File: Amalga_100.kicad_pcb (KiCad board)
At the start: 6 copper layers, 268 x 155 mm, 223 parts, among them IC1 ADM3052, IC3 INA240A1, IC4 INA240A1, IC5 INA240A1, P1 USB_B, P10 IN-, P2 Interface, P3 IN+, P4 IN-, P5 MOTOR3, P6 MOTOR2, P7 MOTOR1, P8 SWD, P9 CONN_6-HSWR-V2-rescue, Q1 IRFP4668PBF, Q10 IRFP4668PBF, Q11 IRFP4668PBF, Q12 IRFP4668PBF, Q13 BC846B, Q14 BC856B, Q15 BC846B, Q16 BC856B, Q2 IRFP4668PBF, Q3 IRFP4668PBF, Q4 IRFP4668PBF, Q5 IRFP4668PBF, Q6 IRFP4668PBF, Q7 IRFP4668PBF, Q8 IRFP4668PBF, Q9 IRFP4668PBF, SW1 SW_DIP_x02, U1 STM32F40X_LQFP64, U10 AD8664ARZ, U2 B1215S-2W, U3 JW5052C, U4 JW5052C, U5 ADUM3160, U6 AD2S1200YSTZ, U7 IRS2186, U8 IRS2186, U9 IRS2186, Y1 8MHz, Y2 8.912 MHZ

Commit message: made Bom (BomAmalga_Kosten.xlsx) Backup
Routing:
- net /Mosfet driver/H1_LOW: vias 62 -> 61
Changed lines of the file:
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@@
-(kicad_pcb (version 20171130) (host pcbnew "(5.0.1)-4")
+(kicad_pcb (version 20171130) (host pcbnew "(5.0.0)")
   (general
     (thickness 1.6)
     (drawings 95)
-    (tracks 3967)
+    (tracks 3965)
     (zones 0)
     (modules 223)
@@
     (tags "DIP Switch Slide 5.08mm 200mil Copal_CHS-A")
     (attr smd)
-    (fp_text reference SW1 (at 0 -2.965 270) (layer F.SilkS)
+    (fp_text reference SW1 (at 0 -0.2) (layer F.SilkS)
       (effects (font (size 1 1) (thickness 0.15)))
     )
@@
     (tags capacitor)
     (attr smd)
-    (fp_text reference C21 (at 0 -1.65 180) (layer F.SilkS)
+    (fp_text reference C21 (at 0.1 -1.9 180) (layer F.SilkS)
       (effects (font (size 1 1) (thickness 0.15)))
     )
@@
     (tags resistor)
     (attr smd)
-    (fp_text reference R67 (at 2.2625 1.6 180) (layer F.SilkS)
+    (fp_text reference R67 (at 2.4625 1.6 180) (layer F.SilkS)
       (effects (font (size 1 1) (thickness 0.15)))
     )
@@
     (tags capacitor)
     (attr smd)
-    (fp_text reference C37 (at -2.3375 0.6) (layer F.SilkS)
+    (fp_text reference C37 (at 2.7625 1) (layer F.SilkS)
       (effects (font (size 1 1) (thickness 0.15)))
     )
@@
     (tags capacitor)
     (attr smd)
-    (fp_text reference C40 (at 2.230367 1.1 180) (layer F.SilkS)
+    (fp_text reference C40 (at 2.230367 0.8 180) (layer F.SilkS)
       (effects (font (size 1 1) (thickness 0.15)))
     )
@@
     (tags resistor)
     (attr smd)
-    (fp_text reference R13 (at -2.330367 1.4) (layer F.SilkS)
+    (fp_text reference R13 (at -2.230367 0.6) (layer F.SilkS)
       (effects (font (size 1 1) (thickness 0.15)))
     )
@@
     (tags capacitor)
     (attr smd)
-    (fp_text reference C72 (at -2.8 1.4 180) (layer F.SilkS)
+    (fp_text reference C72 (at 0.1 1.5 180) (layer F.SilkS)
       (effects (font (size 1 1) (thickness 0.15)))
     )
@@
     (tags capacitor)
     (attr smd)
-    (fp_text reference C70 (at 0 -1.65) (layer F.SilkS)
+    (fp_text reference C70 (at -3 -0.2) (layer F.SilkS)
       (effects (font (size 1 1) (thickness 0.15)))
     )
@@
     (tags capacitor)
     (attr smd)
-    (fp_text reference C8 (at 2.687508 0.023924) (layer F.SilkS)
+    (fp_text reference C8 (at -0.512492 1.623924) (layer F.SilkS)
       (effects (font (size 1 1) (thickness 0.15)))
     )
@@
     (tags "SOIC 1.27")
     (attr smd)
-    (fp_text reference U10 (at -0.369028 2.773084 180) (layer F.SilkS)
+    (fp_text reference U10 (at -5.169028 2.273084 180) (layer F.SilkS)
       (effects (font (size 1 1) (thickness 0.15)))
     )
@@
     (tags SOT-23)
     (attr smd)
-    (fp_text reference Q14 (at -3.045647 1.618975 180) (layer F.SilkS)
+    (fp_text reference Q14 (at -3.345647 0.218975 180) (layer F.SilkS)
       (effects (font (size 1 1) (thickness 0.15)))
     )
@@
     (tags resistor)
     (attr smd)
-    (fp_text reference R42 (at 2.276076 -0.412492 180) (layer F.SilkS)
+    (fp_text reference R42 (at 2.276076 -0.712492 180) (layer F.SilkS)
       (effects (font (size 1 1) (thickness 0.15)))
     )
@@
     (tags resistor)
     (attr smd)
-    (fp_text reference R74 (at 0.2 -1.4625) (layer F.SilkS)
-      (effects (font (size 1 1) (thickness 0.15)))
+    (fp_text reference R74 (at -2.1 0.0375 90) (layer F.SilkS)
+      (effects (font (size 1 0.8) (thickness 0.15)))
     )
     (fp_text value 2K7 (at 0 1.65) (layer F.Fab)
@@
     (tags resistor)
     (attr smd)
-    (fp_text reference R76 (at 0 -1.65) (layer F.SilkS)
-      (effects (font (size 1 1) (thickness 0.15)))
+    (fp_text reference R76 (at -2.134259 0.5375 90) (layer F.SilkS)
+      (effects (font (size 1 0.8) (thickness 0.15)))
     )
     (fp_text value 33R (at 0 1.65) (layer F.Fab)
@@
     (tags resistor)
     (attr smd)
-    (fp_text reference R73 (at 0 -1.65 180) (layer F.SilkS)
+    (fp_text reference R73 (at -3.1 1.7625 180) (layer F.SilkS)
       (effects (font (size 1 1) (thickness 0.15)))
     )
@@
     (tags resistor)
     (attr smd)
-    (fp_text reference R69 (at -2.854353 1.581025) (layer F.SilkS)
+    (fp_text reference R69 (at -3.054353 1.381025) (layer F.SilkS)
       (effects (font (size 1 1) (thickness 0.15)))
     )
@@
     (tags resistor)
     (attr smd)
-    (fp_text reference R68 (at 2.369028 -0.273084 180) (layer F.SilkS)
+    (fp_text reference R68 (at 2.569028 -0.473084 180) (layer F.SilkS)
       (effects (font (size 1 1) (thickness 0.15)))
     )
@@
     (tags resistor)
     (attr smd)
-    (fp_text reference R39 (at -2.3375 1.3) (layer F.SilkS)
+    (fp_text reference R39 (at -0.0375 2.4) (layer F.SilkS)
       (effects (font (size 1 1) (thickness 0.15)))
     )
@@
   (segment (start 169.17003 151.35003) (end 170.674929 152.854929) (width 0.25) (layer "inner_layer4_(Sig)") (net 5))
   (via (at 210.7 80.8) (size 0.6) (drill 0.4) (layers "F.Cu_(top)" "B.Cu_(GND_bottom)") (net 6))
-  (via (at 213.82 92.2) (size 1) (drill 0.6) (layers "F.Cu_(top)" "B.Cu_(GND_bottom)") (net 6) (status 30))
   (segment (start 246.599358 110.411855) (end 236 110.411855) (width 0.25) (layer "F.Cu_(top)") (net 6))
   (segment (start 234.6 106.45) (end 234.6 108.1) (width 0.3) (layer "B.Cu_(GND_bottom)") (net 6) (status 10))
@@
   (segment (start 34.62501 163.87499) (end 34 164.5) (width 0.25) (layer "F.Cu_(top)") (net 163))
   (segment (start 34 164.5) (end 30.6 164.5) (width 0.25) (layer "F.Cu_(top)") (net 163))
-  (segment (start 36.8 161.5375) (end 37.4375 160.9) (width 0.25) (layer "F.Cu_(top)") (net 164))
   (segment (start 37.4375 160.9) (end 38.625 160.9) (width 0.25) (layer "F.Cu_(top)") (net 164))
-  (segment (start 36.6 161.8375) (end 36.8 161.6375) (width 0.25) (layer "F.Cu_(top)") (net 164))
-  (segment (start 36.6 164.1) (end 36.6 161.8375) (width 0.25) (layer "F.Cu_(top)") (net 164))
+  (segment (start 36.6 161.7) (end 37.1 161.2) (width 0.25) (layer "F.Cu_(top)") (net 164))
+  (segment (start 36.6 164.1) (end 36.6 161.7) (width 0.25) (layer "F.Cu_(top)") (net 164))
   (segment (start 35.7 165) (end 36.6 164.1) (width 0.25) (layer "F.Cu_(top)") (net 164))
   (segment (start 30.218147 165) (end 35.7 165) (width 0.25) (layer "F.Cu_(top)") (net 164))
@@
         (xy 61 91.103946) (xy 61.041322 91.104) (xy 61.041322 97.104) (xy 64.041322 100.104) (xy 76.041322 100.104)
         (xy 78.541322 97.604) (xy 78.5 94.75) (xy 91.958678 94.746) (xy 92.039398 100.502076) (xy 92 104)
-        (xy 87.8 108.4) (xy 59.4 108.4) (xy 58 107) (xy 58 84.4) (xy 55.8 82.2)
-        (xy 55.8 79.911341) (xy 61 79.911341)
+        (xy 87.8 108.4) (xy 59.4 108.4) (xy 58 107) (xy 58 90) (xy 61 90)
       )
     )
@@
     (polygon
       (pts
-        (xy 138 91.1) (xy 138.01 91.1) (xy 138.01 97.1) (xy 141.01 100.1) (xy 153.01 100.1)
+        (xy 138 90) (xy 138.01 91.1) (xy 138.01 97.1) (xy 141.01 100.1) (xy 153.01 100.1)
         (xy 155.51 97.6) (xy 155.51 94.5) (xy 169.01 94.5) (xy 169.008076 100.498076) (xy 169.01 103.6)
         (xy 164.2 108.4) (xy 136.4 108.4) (xy 135.01 107.1) (xy 135.01 100.1) (xy 135 100.1)
-        (xy 135 84.4) (xy 132.8 82.2) (xy 132.8 79.9) (xy 138 79.9)
+        (xy 135 90)
       )
     )
@@
         (xy 215.05 97) (xy 218.05 100) (xy 230.05 100) (xy 232.55 97.5) (xy 232.55 94.4)
         (xy 245.45 94.4) (xy 246.05 94.4) (xy 246.048076 100.398076) (xy 246.05 103.5) (xy 241.55 108)
-        (xy 213.05 108) (xy 212.05 107) (xy 212.05 84.3) (xy 209.75 82.2) (xy 209.8 79.900096)
-        (xy 215.1 79.899904)
+        (xy 213.05 108) (xy 212.05 107) (xy 212 90) (xy 215 90)
       )
     )

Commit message: added 2 mounting holes
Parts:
- removed the MH1 at (24.0, 187.0)
- removed SYM2: SYM_Arrow45_Tiny, Symbols:Symbol_Attention_CopperTop_Small
- added MH1: MountingHole, MountingHole:MountingHole_3.2mm_M3_ISO14580_Pad, F.Cu at (277.9, 17.5)
- added MH1: MountingHole, MountingHole:MountingHole_3.2mm_M3_ISO14580_Pad, F.Cu at (19.0, 17.0)
- added MH1: MountingHole, MountingHole:MountingHole_3.2mm_M3_ISO14580_Pad, F.Cu at (19.9, 162.5)
- C31, C32, C33: value 1u -> 1u 600V
- moved SYM1 137.1 mm to (264.6, 156.8)
- moved C53 84.4 mm to (110.8, 50.4)
- moved C51 77.3 mm to (187.9, 50.4)
- moved C50 25.0 mm to (32.4, 50.3)
- moved C19 24.8 mm to (158.0, 143.4)
- moved C27 24.8 mm to (263.9, 130.5)
- moved C41 24.8 mm to (248.3, 81.2)
- moved C5 24.8 mm to (269.4, 133.0)
- moved C54 24.8 mm to (104.9, 53.9)
- moved C61 24.8 mm to (258.9, 54.0)
- moved C62 24.8 mm to (171.3, 81.6)
- moved C63 24.8 mm to (272.9, 54.0)
- moved C66 24.8 mm to (181.9, 53.9)
- moved C69 24.8 mm to (200.4, 158.8)
- moved C7 24.8 mm to (269.4, 130.0)
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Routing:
- net H1_VS: track 159.8 -> 146.0 mm
- net H3_VS: track 221.4 -> 224.2 mm
- net GND: track 452.6 -> 451.2 mm, vias 51 -> 54
- net /MCU/SCK_ADC_EXT: track 164.5 -> 163.8 mm
- net /Resolver/Cos(S2): track 18.5 -> 18.7 mm, vias 1 -> 0
- net +BATT: vias 565 -> 557

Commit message: -tidied up resolver circuit (need voltage detection on reset pin. >10µs, low active)
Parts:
- removed the MH1 at (277.9, 17.5)
- removed the MH1 at (19.0, 17.0)
- added MH11: MountingHole, Mounting_Holes:MountingHole_3.2mm_M3_ISO14580_Pad, F.Cu at (19.0, 17.0)
- added MH12: MountingHole, Mounting_Holes:MountingHole_3.2mm_M3_ISO14580_Pad, F.Cu at (277.9, 17.5)
- MH1, MH2: footprint MountingHole:MountingHole_3.2mm_M3_ISO14580_Pad -> Mounting_Holes:MountingHole_3.2mm_M3_ISO14580_Pad
- MH10, MH3, MH4, MH5, MH6, MH7, MH8, MH9: footprint MountingHole:MountingHole_3.2mm_M3_ISO14580 -> Mounting_Holes:MountingHole_3.2mm_M3_ISO14580
- R61: value 442R -> 442R 1%
- R64: value 1K24 -> 1K24 1%
- U10: footprint Package_SO:SOIC-14_3.9x8.7mm_P1.27mm -> Housings_SOIC:SOIC-14_3.9x8.7mm_Pitch1.27mm
- moved C27 65.0 mm to (198.9, 131.4)
- moved C5 65.0 mm to (204.4, 133.9)
- moved C7 65.0 mm to (204.4, 130.9)
- moved L2 65.0 mm to (201.9, 126.4)
- moved R40 65.0 mm to (208.4, 134.4)
- moved R43 65.0 mm to (199.9, 134.4)
- moved R44 65.0 mm to (197.9, 134.4)
- moved U4 65.0 mm to (204.4, 133.9)
- moved C45 0.65 mm to (68.5, 120.3)
- moved C46 0.56 mm to (104.3, 120.1)
- moved C48 0.25 mm to (53.4, 120.3)
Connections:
- IC1 pad 10: Net-(IC1-Pad10) -> (no net)
- P8 pad 6: Net-(P8-Pad6) -> (no net)
- Q13 pad 3: +12V -> +15V
- Q15 pad 3: +12V -> +15V
- U1 pad 2: Net-(U1-Pad2) -> (no net)
- U1 pad 25: Net-(U1-Pad25) -> (no net)
- U1 pad 28: Net-(U1-Pad28) -> (no net)
- U1 pad 3: Net-(U1-Pad3) -> (no net)
- U1 pad 33: Net-(U1-Pad33) -> (no net)
- U1 pad 4: Net-(U1-Pad4) -> (no net)
- U1 pad 53: Net-(U1-Pad53) -> (no net)
- U1 pad 54: Net-(U1-Pad54) -> (no net)
- U6 pad 10: Net-(U6-Pad10) -> (no net)
- U6 pad 11: Net-(U6-Pad11) -> (no net)
- U6 pad 12: Net-(U6-Pad12) -> (no net)
- U6 pad 13: Net-(U6-Pad13) -> (no net)
- U6 pad 14: Net-(U6-Pad14) -> (no net)
- U6 pad 15: Net-(U6-Pad15) -> (no net)
- U6 pad 16: Net-(U6-Pad16) -> GND
- U6 pad 18: Net-(U6-Pad18) -> (no net)
- U6 pad 19: Net-(U6-Pad19) -> (no net)
- U6 pad 20: Net-(U6-Pad20) -> (no net)
- U6 pad 24: Net-(U6-Pad24) -> (no net)
- U6 pad 29: Net-(U6-Pad29) -> (no net)
- U6 pad 30: Net-(U6-Pad30) -> (no net)
- U6 pad 33: Net-(U6-Pad33) -> (no net)
- U6 pad 44: Net-(U6-Pad44) -> (no net)
- U6 pad 9: Net-(U6-Pad9) -> (no net)
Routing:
- net +15V: track 528.0 -> 492.2 mm, vias 9 -> 10
- net +12V: track 25.9 -> 0.00 mm
- net +3V3: track 620.7 -> 607.8 mm, vias 14 -> 15
- net H1_VS: track 146.0 -> 152.8 mm
- net GND: track 451.2 -> 448.5 mm, vias 54 -> 53
- net GNDPWR: track 81.9 -> 84.2 mm
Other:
- board text added: "Amalga 600V 150A *20190213"
- board text added: "prim. to sec. Ohm 1:2 100k 1:1 40k 2:1 10k 5:1"
- board text removed: "Amalga 200 600V 150A *20190213 -Orig A.S."
- board text removed: "prim. to sec. Ohm 1:1 100k 2:1 40k 5:1 10k"

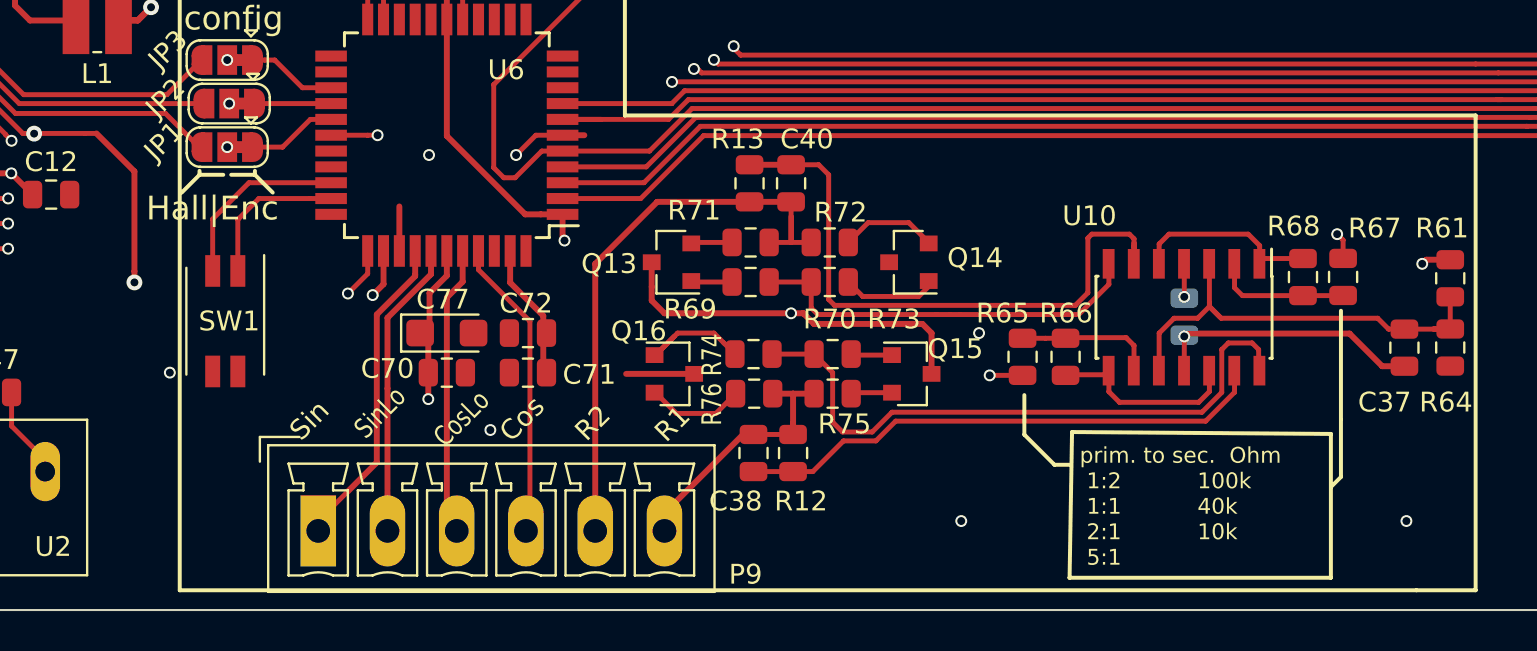
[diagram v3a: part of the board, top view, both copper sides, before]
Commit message: -started implementing new sin/cos-Encoder Inputs -small changes like silkscreen
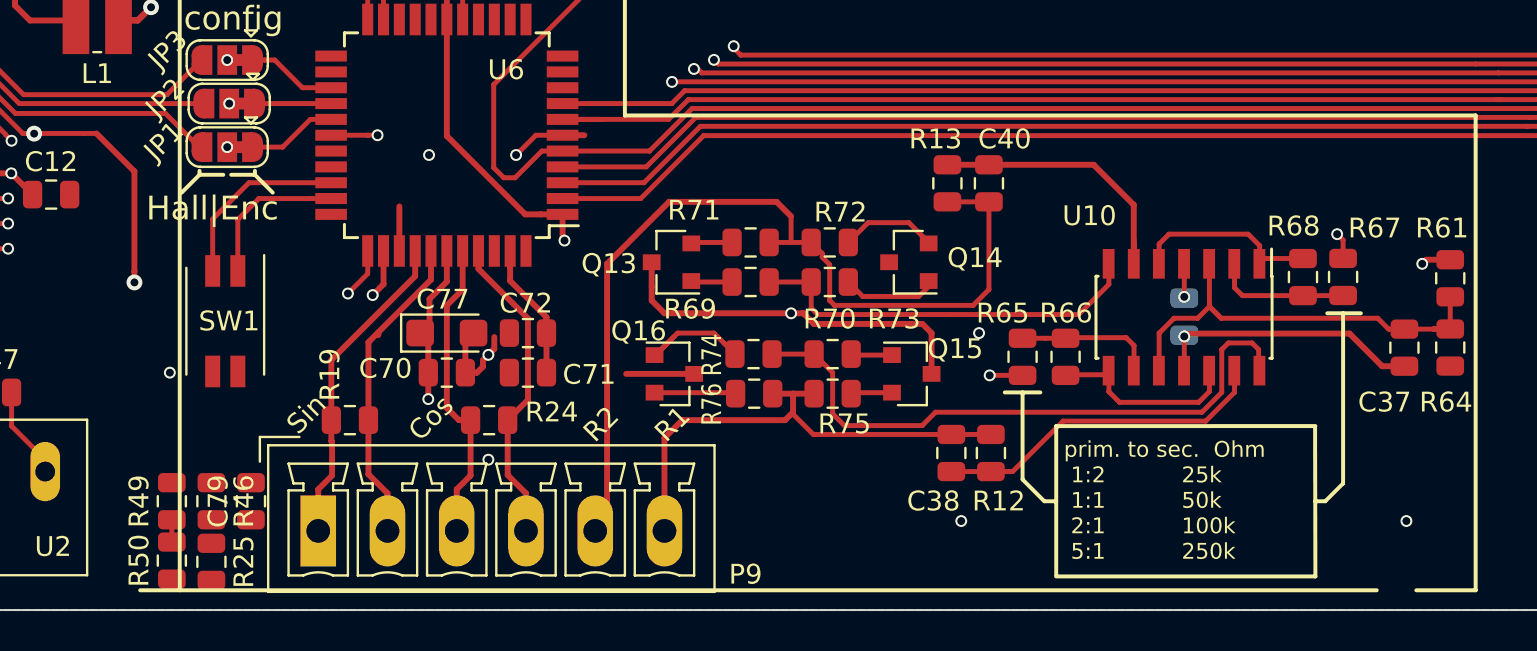
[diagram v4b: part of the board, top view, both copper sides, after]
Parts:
- added C79: 10nF, Capacitor_SMD:C_0805_2012Metric, F.Cu at (80.0, 162.0)
- added R19: 68k, Resistor_SMD:R_0805_2012Metric, F.Cu at (85.0, 157.9)
- added R24: 68k, Resistor_SMD:R_0805_2012Metric, F.Cu at (92.0, 157.9)
- added R25: 68k, Resistor_SMD:R_0805_2012Metric, F.Cu at (78.0, 165.1)
- added R46: 68k, Resistor_SMD:R_0805_2012Metric, F.Cu at (78.0, 162.0)
- added R49: 68k, Resistor_SMD:R_0805_2012Metric, F.Cu at (76.0, 162.0)
- added R50: 68k, Resistor_SMD:R_0805_2012Metric, F.Cu at (76.0, 165.0)
- R65, R67: value ?R -> 100k 1%
- R66, R68: value ?R -> 25k 1%
- moved C38 10.0 mm to (115.4, 159.6)
- moved C40 10.0 mm to (117.3, 145.9)
- moved R12 10.0 mm to (117.4, 159.6)
- moved R13 10.0 mm to (115.2, 145.9)
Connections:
- net SPI1_SCK(R2D) renamed SPI1_SCK_(R2D)
- IC1 pad 10: (no net) -> Net-(IC1-Pad10)
- P8 pad 6: (no net) -> Net-(P8-Pad6)
- U1 pad 2: (no net) -> /Resolver/*RDvel
- U1 pad 25: (no net) -> Net-(U1-Pad25)
- U1 pad 26: /Resolver/*CS -> /MCU/SIN_IN_RES
- U1 pad 27: /Resolver/*RDvel -> /MCU/COS_IN_RES
- U1 pad 28: (no net) -> Net-(U1-Pad28)
- U1 pad 3: (no net) -> Net-(U1-Pad3)
- U1 pad 33: (no net) -> Net-(U1-Pad33)
- U1 pad 4: (no net) -> Net-(U1-Pad4)
- U1 pad 53: (no net) -> /Resolver/*CS
- U1 pad 54: (no net) -> Net-(U1-Pad54)
- U6 pad 10: (no net) -> Net-(U6-Pad10)
- U6 pad 11: (no net) -> Net-(U6-Pad11)
- U6 pad 12: (no net) -> Net-(U6-Pad12)
- U6 pad 13: (no net) -> Net-(U6-Pad13)
- U6 pad 14: (no net) -> Net-(U6-Pad14)
- U6 pad 15: (no net) -> Net-(U6-Pad15)
- U6 pad 18: (no net) -> Net-(U6-Pad18)
- U6 pad 19: (no net) -> Net-(U6-Pad19)
- U6 pad 20: (no net) -> Net-(U6-Pad20)
- U6 pad 24: (no net) -> Net-(U6-Pad24)
- U6 pad 29: (no net) -> Net-(U6-Pad29)
- U6 pad 30: (no net) -> Net-(U6-Pad30)
- U6 pad 33: (no net) -> Net-(U6-Pad33)
- U6 pad 44: (no net) -> Net-(U6-Pad44)
- U6 pad 9: (no net) -> Net-(U6-Pad9)
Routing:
- net /Resolver/*CS: track 76.7 -> 4.11 mm, vias 2 -> 0
- net /MCU/SIN_IN_RES: track 0.00 -> 72.6 mm, vias 0 -> 2
- net /Resolver/*RDvel: track 93.2 -> 21.1 mm, vias 2 -> 0
- net /MCU/COS_IN_RES: track 0.00 -> 72.2 mm, vias 0 -> 2
- net /Resolver/R2: track 31.4 -> 47.7 mm
- net Net-(C40-Pad2): track 31.5 -> 15.5 mm
- net /Resolver/R1: track 14.1 -> 26.7 mm
- net Net-(C38-Pad2): track 27.1 -> 18.1 mm, vias 0 -> 1
- net GND: track 448.5 -> 453.4 mm
- net /Resolver/CosLO(S6): track 16.8 -> 19.4 mm
- net /Resolver/Sin(S1): track 15.0 -> 16.2 mm
- net /Resolver/SinLO(S3): track 15.0 -> 16.0 mm
- net /Resolver/Cos(S2): track 18.7 -> 19.7 mm
- net Net-(Q16-Pad2): track 4.95 -> 4.12 mm
- net Net-(R73-Pad2): track 32.5 -> 32.0 mm
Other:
- board text added: "prim. to sec. Ohm 1:2 25k 1:1 50k 2:1 100k 5:1 250k"
- board text removed: "CosLo"
- board text removed: "SinLo"
- board text removed: "prim. to sec. Ohm 1:2 100k 1:1 40k 2:1 10k 5:1"
